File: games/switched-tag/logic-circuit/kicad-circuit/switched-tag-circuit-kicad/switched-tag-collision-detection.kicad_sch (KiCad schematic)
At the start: 25 parts

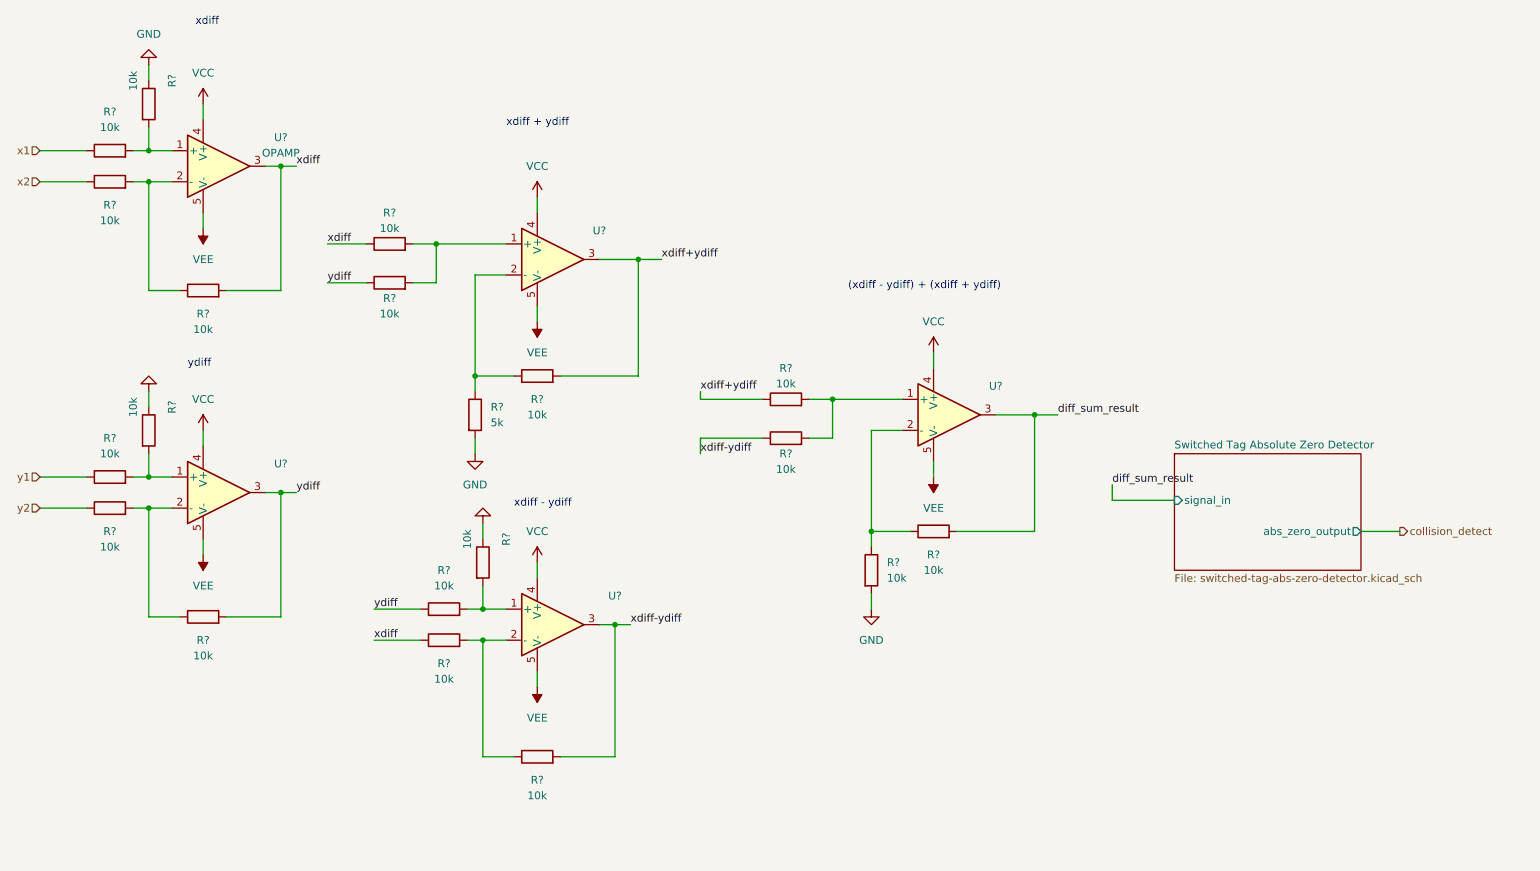
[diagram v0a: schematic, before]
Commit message: Saving progress on kicad schematic. Trying to set up ngspice simulation.
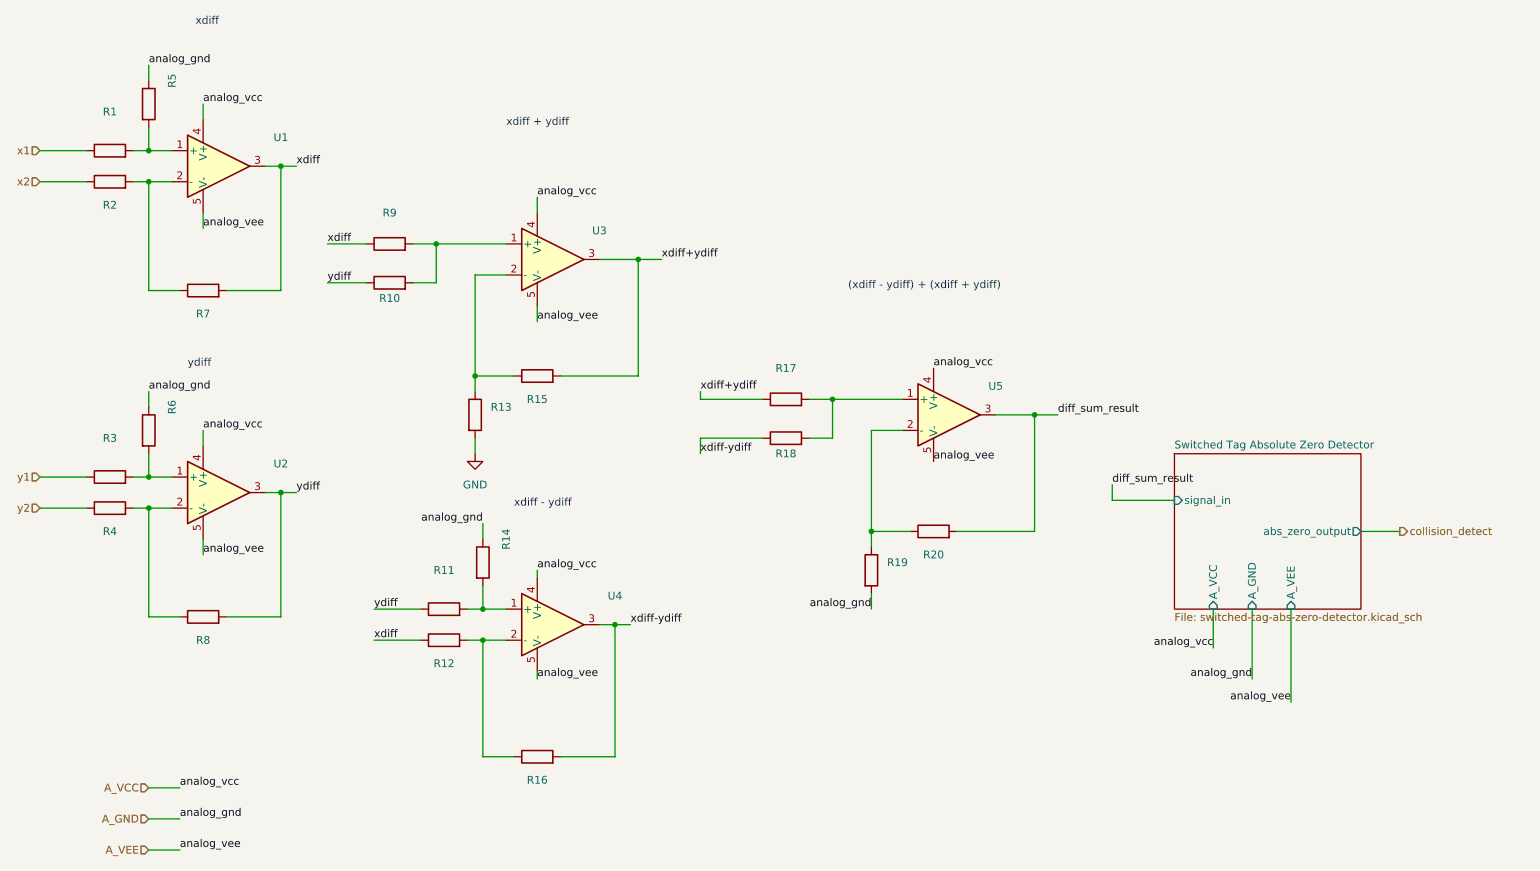
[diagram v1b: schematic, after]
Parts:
- R1, R10, R11, R12, R14, R15, R16, R17, R18, R19, R2, R20, R3, R4, R5, R6, R7, R8, R9: renamed from R?; value 10k -> (none)
- R13: renamed from R?; value 5k -> (none)
- U1: renamed from U?; value OPAMP -> (none); Spice_Lib_File (none) -> /home/pab/Inventions/analog-circuit-game-console/ms-circuit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; Spice_Model (none) -> LM358; Spice_Node_Sequence (none) -> 1 2 4 5 3
- U2, U3, U4, U5: renamed from U?; value ~ -> (none); Spice_Lib_File (none) -> /home/pab/Inventions/analog-circuit-game-console/ms-circuit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; Spice_Model (none) -> LM358; Spice_Node_Sequence (none) -> 1 2 4 5 3
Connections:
- net GND: no longer R14.1, R19.2, R5.1, R6.1
- net VCC renamed A_VCC
- net VEE renamed A_VEE
- new net A_GND: R14.1, R19.2, R5.1, R6.1
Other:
- sheet Switched Tag Absolute Zero Detector ports: added A_GND, A_VCC, A_VEE; removed none

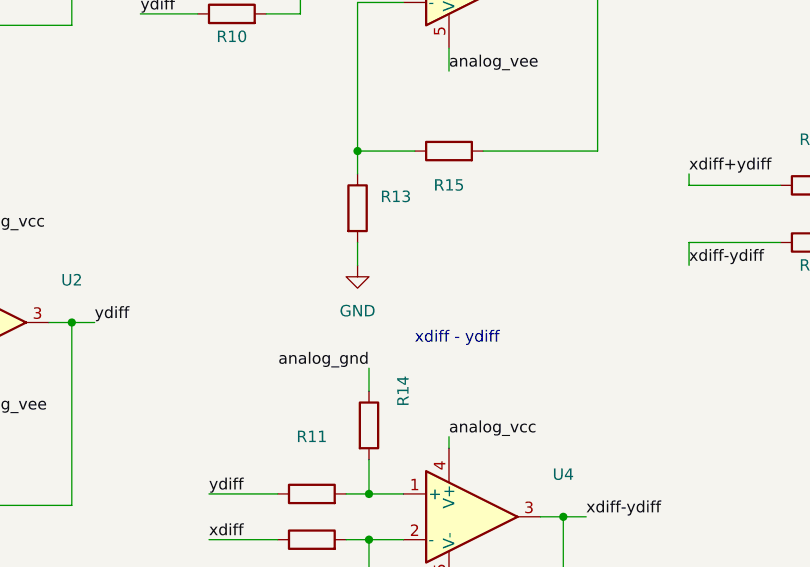
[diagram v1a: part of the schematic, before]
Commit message: Fixed problems with kicad circuit adn spice setup.
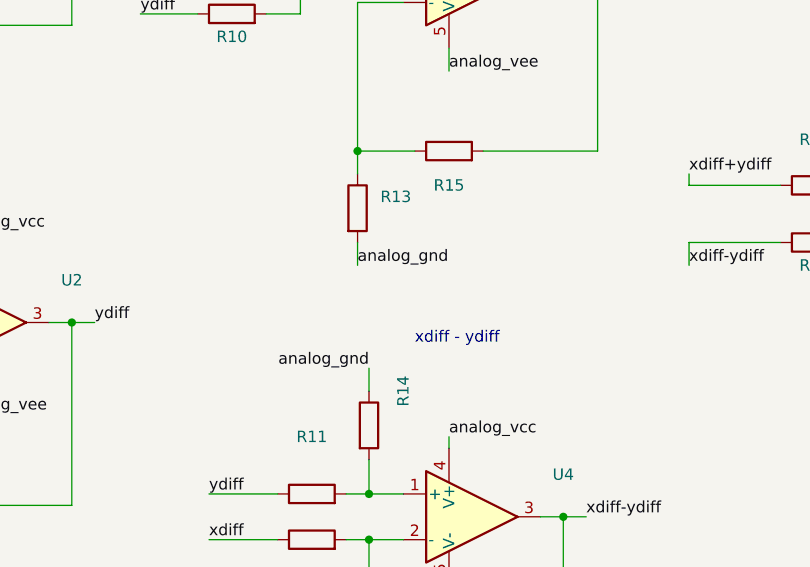
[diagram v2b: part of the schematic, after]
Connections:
- net GND is gone; now on net A_GND: R13.2
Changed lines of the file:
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@@
     (effects (font (size 1.27 1.27)) (justify right bottom))
+  )
+  (label "analog_gnd" (at 91.44 97.79 0)
+    (effects (font (size 1.27 1.27)) (justify left bottom))
   )
   (label "ydiff" (at 62.23 104.14 0)
@@
     (pin "5")
   )
-  (symbol (lib_id "power:GND") (at 91.44 97.79 0) (unit 1)
-    (in_bom yes) (on_board yes) (fields_autoplaced)
-    (property "Reference" "#PWR019" (id 0) (at 91.44 104.14 0)
-      (effects (font (size 1.27 1.27)) hide)
-    )
-    (property "Value" "GND" (id 1) (at 91.44 102.87 0))
-    (property "Footprint" "" (id 2) (at 91.44 97.79 0)
-      (effects (font (size 1.27 1.27)) hide)
-    )
-    (property "Datasheet" "" (id 3) (at 91.44 97.79 0)
-      (effects (font (size 1.27 1.27)) hide)
-    )
-    (pin "1")
-  )
   (symbol (lib_id "Device:R") (at 38.1 93.98 0) (unit 1)

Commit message: Changed spice model of opamp in kicad sim. Fixed design error in it player determination in ltspice and kicad schematic
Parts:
- U1, U2, U3, U4, U5: Spice_Lib_File /home/pab/Inventions/analog-circuit-game-console/ms-circuit-video-games/spice-models/LM358-onsemi.mod -> /home/pab/Inventions/analog-circuit-game-console/ms-circuit-video-games/spice-models/ada4692.mod; Spice_Model LM358 -> ADA4692
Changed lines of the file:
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@@
       (effects (font (size 1.27 1.27)) (justify left) hide)
     )
-    (property "Spice_Model" "LM358" (id 6) (at 168.91 91.44 0)
+    (property "Spice_Model" "ADA4692" (id 6) (at 168.91 91.44 0)
       (effects (font (size 1.27 1.27)) hide)
     )
-    (property "Spice_Lib_File" "/home/pab/Inventions/analog-circuit-game-console/ms-circuit-video-games/spice-models/LM358-onsemi.mod" (id 7) (at 168.91 91.44 0)
+    (property "Spice_Lib_File" "/home/pab/Inventions/analog-circuit-game-console/ms-circuit-video-games/spice-models/ada4692.mod" (id 7) (at 168.91 91.44 0)
       (effects (font (size 1.27 1.27)) hide)
     )
@@
       (effects (font (size 1.27 1.27)) (justify left) hide)
     )
-    (property "Spice_Model" "LM358" (id 6) (at 104.14 66.04 0)
+    (property "Spice_Model" "ADA4692" (id 6) (at 104.14 66.04 0)
       (effects (font (size 1.27 1.27)) hide)
     )
-    (property "Spice_Lib_File" "/home/pab/Inventions/analog-circuit-game-console/ms-circuit-video-games/spice-models/LM358-onsemi.mod" (id 7) (at 104.14 66.04 0)
+    (property "Spice_Lib_File" "/home/pab/Inventions/analog-circuit-game-console/ms-circuit-video-games/spice-models/ada4692.mod" (id 7) (at 104.14 66.04 0)
       (effects (font (size 1.27 1.27)) hide)
     )
@@
       (effects (font (size 1.27 1.27)) (justify left) hide)
     )
-    (property "Spice_Model" "LM358" (id 6) (at 49.53 104.14 0)
+    (property "Spice_Model" "ADA4692" (id 6) (at 49.53 104.14 0)
       (effects (font (size 1.27 1.27)) hide)
     )
-    (property "Spice_Lib_File" "/home/pab/Inventions/analog-circuit-game-console/ms-circuit-video-games/spice-models/LM358-onsemi.mod" (id 7) (at 49.53 104.14 0)
+    (property "Spice_Lib_File" "/home/pab/Inventions/analog-circuit-game-console/ms-circuit-video-games/spice-models/ada4692.mod" (id 7) (at 49.53 104.14 0)
       (effects (font (size 1.27 1.27)) hide)
     )
@@
       (effects (font (size 1.27 1.27)) (justify left) hide)
     )
-    (property "Spice_Model" "LM358" (id 6) (at 104.14 125.73 0)
+    (property "Spice_Model" "ADA4692" (id 6) (at 104.14 125.73 0)
       (effects (font (size 1.27 1.27)) hide)
     )
-    (property "Spice_Lib_File" "/home/pab/Inventions/analog-circuit-game-console/ms-circuit-video-games/spice-models/LM358-onsemi.mod" (id 7) (at 104.14 125.73 0)
+    (property "Spice_Lib_File" "/home/pab/Inventions/analog-circuit-game-console/ms-circuit-video-games/spice-models/ada4692.mod" (id 7) (at 104.14 125.73 0)
       (effects (font (size 1.27 1.27)) hide)
     )
@@
       (effects (font (size 1.27 1.27)) (justify left) hide)
     )
-    (property "Spice_Model" "LM358" (id 6) (at 49.53 50.8 0)
+    (property "Spice_Model" "ADA4692" (id 6) (at 49.53 50.8 0)
       (effects (font (size 1.27 1.27)) hide)
     )
-    (property "Spice_Lib_File" "/home/pab/Inventions/analog-circuit-game-console/ms-circuit-video-games/spice-models/LM358-onsemi.mod" (id 7) (at 49.53 50.8 0)
+    (property "Spice_Lib_File" "/home/pab/Inventions/analog-circuit-game-console/ms-circuit-video-games/spice-models/ada4692.mod" (id 7) (at 49.53 50.8 0)
       (effects (font (size 1.27 1.27)) hide)
     )

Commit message: Added some prep work for console hardware.
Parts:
- U1, U2, U3, U4, U5: Spice_Lib_File /home/pab/Inventions/analog-circuit-game-console/ms-circuit-video-games/spice-models/ada4692.mod -> /home/pab/Inventions/analog-circuit-game-console/ms-circuit-video-games/spice-models/lmx58_lm2904.lib; Spice_Model ADA4692 -> LMX58_LM2904
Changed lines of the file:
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@@
       (effects (font (size 1.27 1.27)) (justify left) hide)
     )
-    (property "Spice_Model" "ADA4692" (id 6) (at 168.91 91.44 0)
+    (property "Spice_Model" "LMX58_LM2904" (id 6) (at 168.91 91.44 0)
       (effects (font (size 1.27 1.27)) hide)
     )
-    (property "Spice_Lib_File" "/home/pab/Inventions/analog-circuit-game-console/ms-circuit-video-games/spice-models/ada4692.mod" (id 7) (at 168.91 91.44 0)
+    (property "Spice_Lib_File" "/home/pab/Inventions/analog-circuit-game-console/ms-circuit-video-games/spice-models/lmx58_lm2904.lib" (id 7) (at 168.91 91.44 0)
       (effects (font (size 1.27 1.27)) hide)
     )
@@
       (effects (font (size 1.27 1.27)) (justify left) hide)
     )
-    (property "Spice_Model" "ADA4692" (id 6) (at 104.14 66.04 0)
+    (property "Spice_Model" "LMX58_LM2904" (id 6) (at 104.14 66.04 0)
       (effects (font (size 1.27 1.27)) hide)
     )
-    (property "Spice_Lib_File" "/home/pab/Inventions/analog-circuit-game-console/ms-circuit-video-games/spice-models/ada4692.mod" (id 7) (at 104.14 66.04 0)
+    (property "Spice_Lib_File" "/home/pab/Inventions/analog-circuit-game-console/ms-circuit-video-games/spice-models/lmx58_lm2904.lib" (id 7) (at 104.14 66.04 0)
       (effects (font (size 1.27 1.27)) hide)
     )
@@
       (effects (font (size 1.27 1.27)) (justify left) hide)
     )
-    (property "Spice_Model" "ADA4692" (id 6) (at 49.53 104.14 0)
+    (property "Spice_Model" "LMX58_LM2904" (id 6) (at 49.53 104.14 0)
       (effects (font (size 1.27 1.27)) hide)
     )
-    (property "Spice_Lib_File" "/home/pab/Inventions/analog-circuit-game-console/ms-circuit-video-games/spice-models/ada4692.mod" (id 7) (at 49.53 104.14 0)
+    (property "Spice_Lib_File" "/home/pab/Inventions/analog-circuit-game-console/ms-circuit-video-games/spice-models/lmx58_lm2904.lib" (id 7) (at 49.53 104.14 0)
       (effects (font (size 1.27 1.27)) hide)
     )
@@
       (effects (font (size 1.27 1.27)) (justify left) hide)
     )
-    (property "Spice_Model" "ADA4692" (id 6) (at 104.14 125.73 0)
+    (property "Spice_Model" "LMX58_LM2904" (id 6) (at 104.14 125.73 0)
       (effects (font (size 1.27 1.27)) hide)
     )
-    (property "Spice_Lib_File" "/home/pab/Inventions/analog-circuit-game-console/ms-circuit-video-games/spice-models/ada4692.mod" (id 7) (at 104.14 125.73 0)
+    (property "Spice_Lib_File" "/home/pab/Inventions/analog-circuit-game-console/ms-circuit-video-games/spice-models/lmx58_lm2904.lib" (id 7) (at 104.14 125.73 0)
       (effects (font (size 1.27 1.27)) hide)
     )
@@
       (effects (font (size 1.27 1.27)) (justify left) hide)
     )
-    (property "Spice_Model" "ADA4692" (id 6) (at 49.53 50.8 0)
+    (property "Spice_Model" "LMX58_LM2904" (id 6) (at 49.53 50.8 0)
       (effects (font (size 1.27 1.27)) hide)
     )
-    (property "Spice_Lib_File" "/home/pab/Inventions/analog-circuit-game-console/ms-circuit-video-games/spice-models/ada4692.mod" (id 7) (at 49.53 50.8 0)
+    (property "Spice_Lib_File" "/home/pab/Inventions/analog-circuit-game-console/ms-circuit-video-games/spice-models/lmx58_lm2904.lib" (id 7) (at 49.53 50.8 0)
       (effects (font (size 1.27 1.27)) hide)
     )

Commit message: Saving progress.
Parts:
- U1, U2, U3, U4, U5: Spice_Lib_File /home/pab/Inventions/analog-circuit-game-console/ms-circuit-video-games/spice-models/lmx58_lm2904.lib -> /home/pab/Inventions/analog-circuit-game-console/ms-circuit-video-games/spice-models/ad8031.mod; Spice_Model LMX58_LM2904 -> AD8031
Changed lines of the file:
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@@
       (effects (font (size 1.27 1.27)) (justify left) hide)
     )
-    (property "Spice_Model" "LMX58_LM2904" (id 6) (at 168.91 91.44 0)
+    (property "Spice_Model" "AD8031" (id 6) (at 168.91 91.44 0)
       (effects (font (size 1.27 1.27)) hide)
     )
-    (property "Spice_Lib_File" "/home/pab/Inventions/analog-circuit-game-console/ms-circuit-video-games/spice-models/lmx58_lm2904.lib" (id 7) (at 168.91 91.44 0)
+    (property "Spice_Lib_File" "/home/pab/Inventions/analog-circuit-game-console/ms-circuit-video-games/spice-models/ad8031.mod" (id 7) (at 168.91 91.44 0)
       (effects (font (size 1.27 1.27)) hide)
     )
@@
       (effects (font (size 1.27 1.27)) (justify left) hide)
     )
-    (property "Spice_Model" "LMX58_LM2904" (id 6) (at 104.14 66.04 0)
+    (property "Spice_Model" "AD8031" (id 6) (at 104.14 66.04 0)
       (effects (font (size 1.27 1.27)) hide)
     )
-    (property "Spice_Lib_File" "/home/pab/Inventions/analog-circuit-game-console/ms-circuit-video-games/spice-models/lmx58_lm2904.lib" (id 7) (at 104.14 66.04 0)
+    (property "Spice_Lib_File" "/home/pab/Inventions/analog-circuit-game-console/ms-circuit-video-games/spice-models/ad8031.mod" (id 7) (at 104.14 66.04 0)
       (effects (font (size 1.27 1.27)) hide)
     )
@@
       (effects (font (size 1.27 1.27)) (justify left) hide)
     )
-    (property "Spice_Model" "LMX58_LM2904" (id 6) (at 49.53 104.14 0)
+    (property "Spice_Model" "AD8031" (id 6) (at 49.53 104.14 0)
       (effects (font (size 1.27 1.27)) hide)
     )
-    (property "Spice_Lib_File" "/home/pab/Inventions/analog-circuit-game-console/ms-circuit-video-games/spice-models/lmx58_lm2904.lib" (id 7) (at 49.53 104.14 0)
+    (property "Spice_Lib_File" "/home/pab/Inventions/analog-circuit-game-console/ms-circuit-video-games/spice-models/ad8031.mod" (id 7) (at 49.53 104.14 0)
       (effects (font (size 1.27 1.27)) hide)
     )
@@
       (effects (font (size 1.27 1.27)) (justify left) hide)
     )
-    (property "Spice_Model" "LMX58_LM2904" (id 6) (at 104.14 125.73 0)
+    (property "Spice_Model" "AD8031" (id 6) (at 104.14 125.73 0)
       (effects (font (size 1.27 1.27)) hide)
     )
-    (property "Spice_Lib_File" "/home/pab/Inventions/analog-circuit-game-console/ms-circuit-video-games/spice-models/lmx58_lm2904.lib" (id 7) (at 104.14 125.73 0)
+    (property "Spice_Lib_File" "/home/pab/Inventions/analog-circuit-game-console/ms-circuit-video-games/spice-models/ad8031.mod" (id 7) (at 104.14 125.73 0)
       (effects (font (size 1.27 1.27)) hide)
     )
@@
       (effects (font (size 1.27 1.27)) (justify left) hide)
     )
-    (property "Spice_Model" "LMX58_LM2904" (id 6) (at 49.53 50.8 0)
+    (property "Spice_Model" "AD8031" (id 6) (at 49.53 50.8 0)
       (effects (font (size 1.27 1.27)) hide)
     )
-    (property "Spice_Lib_File" "/home/pab/Inventions/analog-circuit-game-console/ms-circuit-video-games/spice-models/lmx58_lm2904.lib" (id 7) (at 49.53 50.8 0)
+    (property "Spice_Lib_File" "/home/pab/Inventions/analog-circuit-game-console/ms-circuit-video-games/spice-models/ad8031.mod" (id 7) (at 49.53 50.8 0)
       (effects (font (size 1.27 1.27)) hide)
     )
